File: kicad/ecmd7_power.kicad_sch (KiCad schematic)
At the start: 74 parts, among them Q10 BSC098N10NS5, Q7 BSC098N10NS5, Q8 BSC098N10NS5, Q9 BSC098N10NS5, U14 LM5118MH, U3 LM5118MH, U6 TLV71318PDBV, U9 LT1616ES6#TRPBF

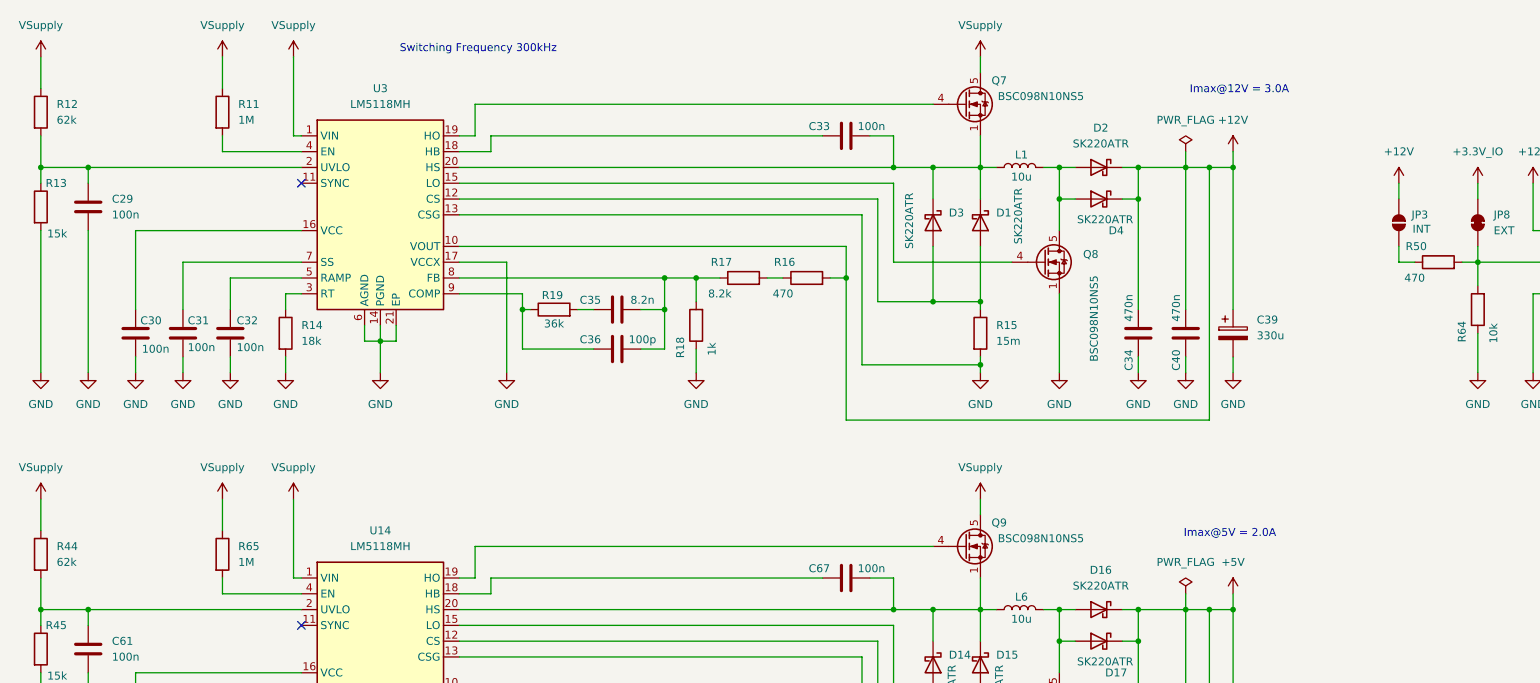
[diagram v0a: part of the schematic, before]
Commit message: Update project structure for enhancment with firmware and software
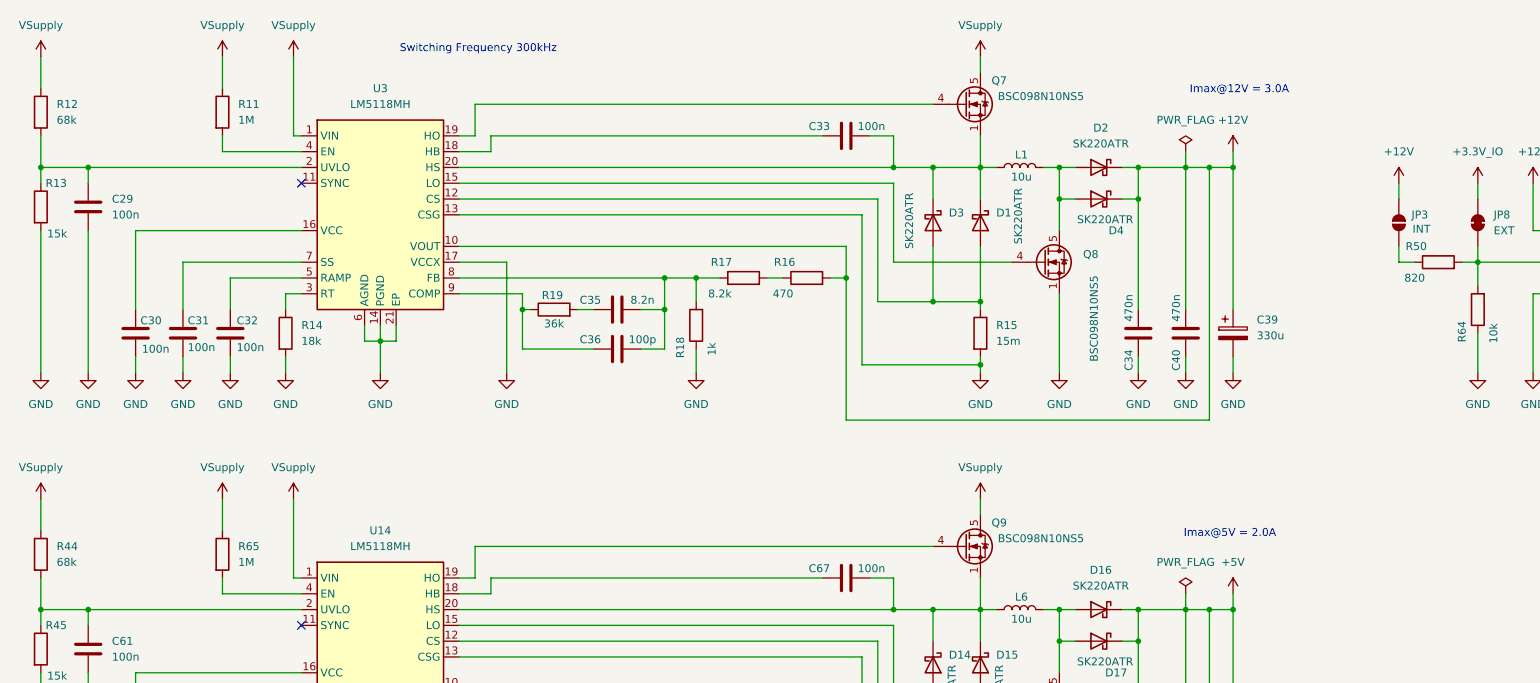
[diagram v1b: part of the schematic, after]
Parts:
- L1, L2, L5, L6: Mouser Part Number (none) -> 851-0530CDMCCDS100MC
- R12, R44: value 62k -> 68k
- R50: value 470 -> 820
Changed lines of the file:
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@@
 			)
 		)
+		(property "Mouser Part Number" "851-0530CDMCCDS100MC"
+			(at 337.82 144.78 90)
+			(effects
+				(font
+					(size 1.27 1.27)
+				)
+				(hide yes)
+			)
+		)
 		(pin "2"
 		)
@@
 			)
 		)
-		(property "Value" "470"
+		(property "Value" "820"
 			(at 271.78 147.32 90)
 			(effects
@@
 			)
 		)
-		(property "Value" "62k"
+		(property "Value" "68k"
 			(at 53.34 121.9199 0)
 			(effects
@@
 			)
 		)
+		(property "Mouser Part Number" "851-0530CDMCCDS100MC"
+			(at 208.28 129.54 90)
+			(effects
+				(font
+					(size 1.27 1.27)
+				)
+				(hide yes)
+			)
+		)
 		(pin "2"
 		)
@@
 			)
 		)
+		(property "Mouser Part Number" "851-0530CDMCCDS100MC"
+			(at 208.28 200.66 90)
+			(effects
+				(font
+					(size 1.27 1.27)
+				)
+				(hide yes)
+			)
+		)
 		(pin "2"
 		)
@@
 			)
 		)
-		(property "Value" "62k"
+		(property "Value" "68k"
 			(at 53.34 193.0399 0)
 			(effects
@@
 			(at 57.15 74.93 90)
 			(effects
+				(font
+					(size 1.27 1.27)
+				)
+				(hide yes)
+			)
+		)
+		(property "Mouser Part Number" "851-0530CDMCCDS100MC"
+			(at 57.15 74.93 90)
+			(effects

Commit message: Cleanup schematic
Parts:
- added D18: 3.3V, Diode_SMD:D_0805_2012Metric, symbol Device:LED
- added D5: 12V, Diode_SMD:D_0805_2012Metric, symbol Device:LED
- added D6: 5V, Diode_SMD:D_0805_2012Metric, symbol Device:LED
- added J6: 12V, Connector_PinSocket_2.54mm:PinSocket_1x02_P2.54mm_Vertical, symbol Connector:Conn_01x02_Socket
- added J8: 5V, Connector_PinSocket_2.54mm:PinSocket_1x02_P2.54mm_Vertical, symbol Connector:Conn_01x02_Socket
- added R46: 4.7k, Resistor_SMD:R_0805_2012Metric, symbol Device:R
- added R47: 1.5k, Resistor_SMD:R_0805_2012Metric, symbol Device:R
- added R48: 330, Resistor_SMD:R_0805_2012Metric, symbol Device:R
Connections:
- net +12V: now also J6.1 (Pin_1), R46.2
- net +3.3V: now also R48.2
- net +5V: now also J8.1 (Pin_1), R47.2
- net GND: now also D18.1 (K), D5.1 (K), D6.1 (K), J6.2 (Pin_2), J8.2 (Pin_2)
- new net: D18.2 (A), R48.1
- new net: D6.2 (A), R47.1
- new net: D5.2 (A), R46.1
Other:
- moved on the sheet: C29, C30, C31, C32, C33, C34, C35, C36, C37, C38, C39, C40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

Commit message: Cleanup schematic, add busses
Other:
- title: (none) -> ECMD7 Power Supplies
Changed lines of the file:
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@@
 	(generator_version "9.0")
 	(paper "A3")
+	(title_block
+		(title "ECMD7 Power Supplies")
+		(date "2025-11-12")
+		(rev "1.0")
+	)
 	(text "Imax@3.3V = 400mA"
 		(exclude_from_sim no)
@@
 				(font
 					(size 1.27 1.27)
-					(italic yes)
 				)
 				(hide yes)

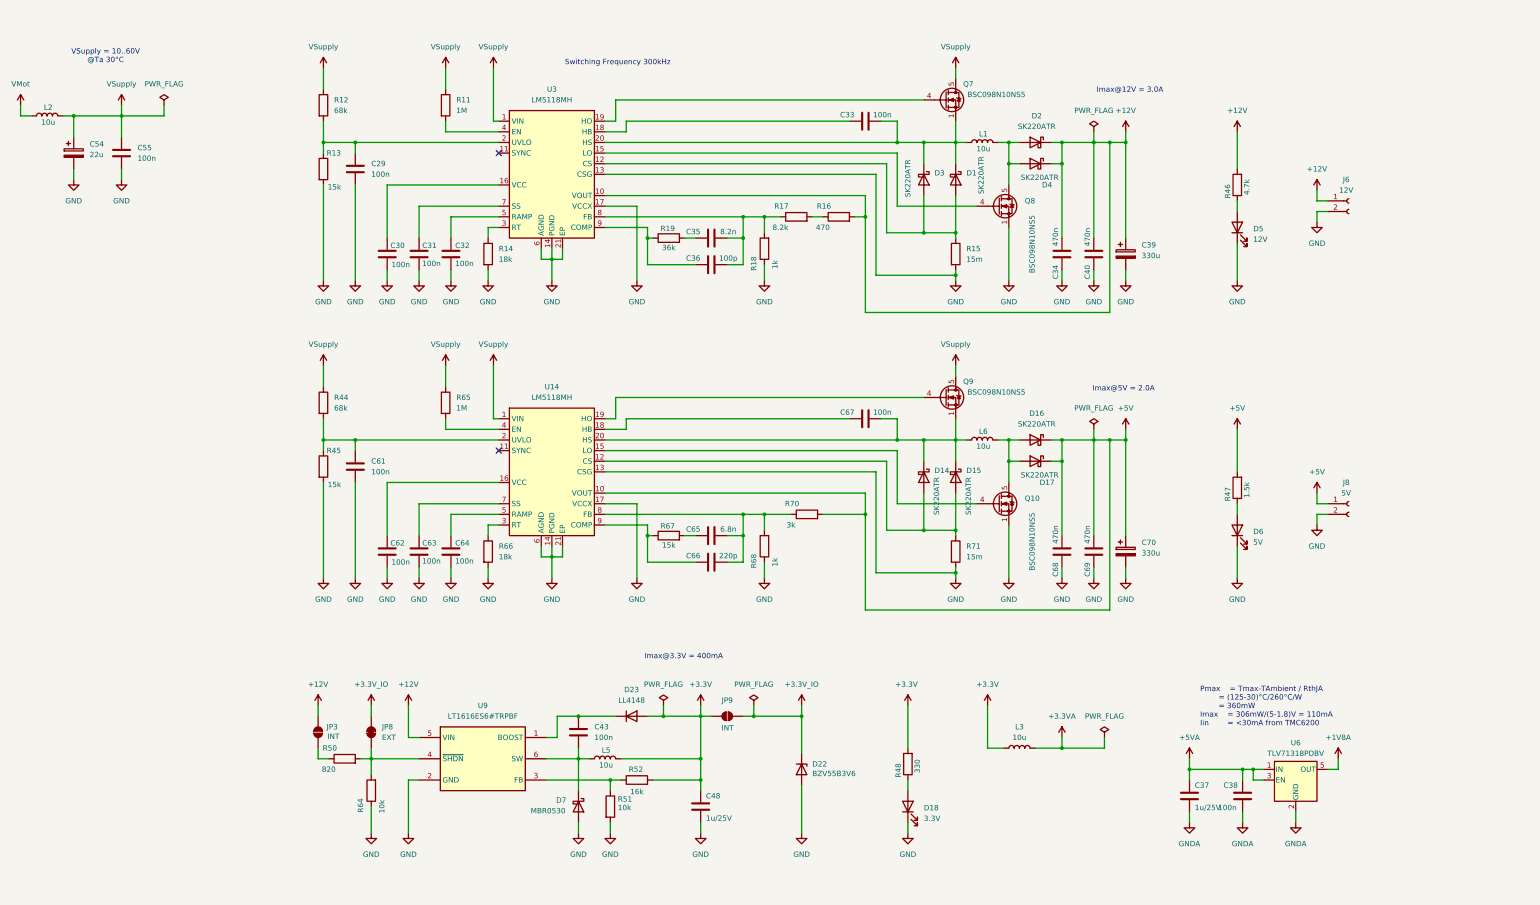
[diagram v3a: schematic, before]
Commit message: General schematic cleanup
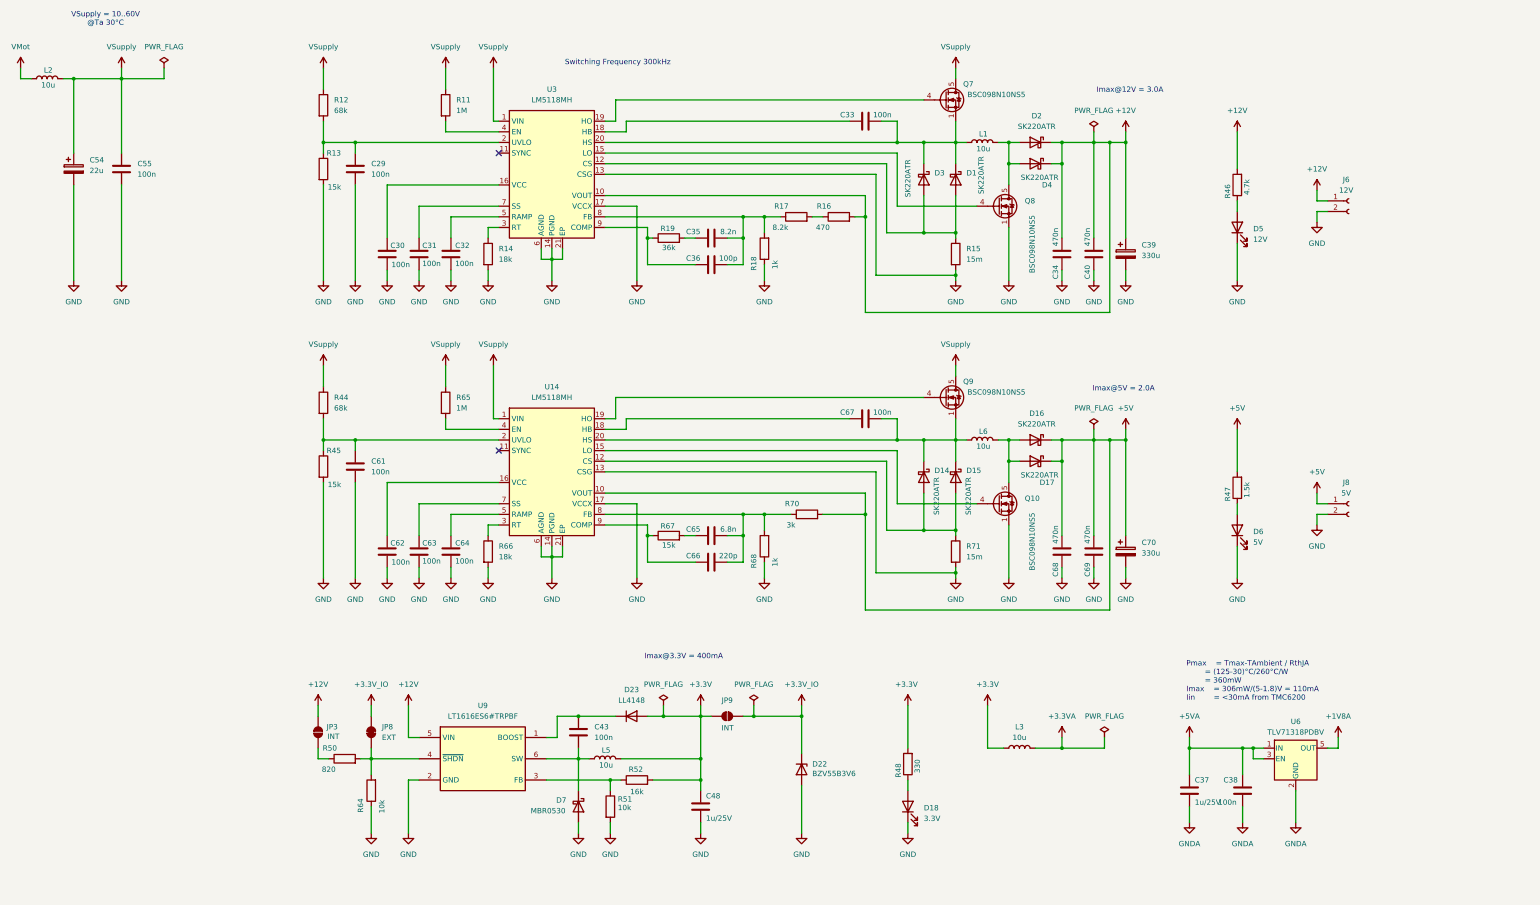
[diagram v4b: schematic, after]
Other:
- moved on the sheet: C37, C38, C54, C55, L2, U6
